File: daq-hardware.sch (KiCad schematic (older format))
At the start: 29 parts, among them J1 USB_B, J2 Micro_SD_Card_Det_Hirose_DM3AT, Q1 MMDT2222A, SW1 SW1, SW2 SW1, U1 CP2102N-A01-GQFN24, U2 ESP32-WROOM-32D

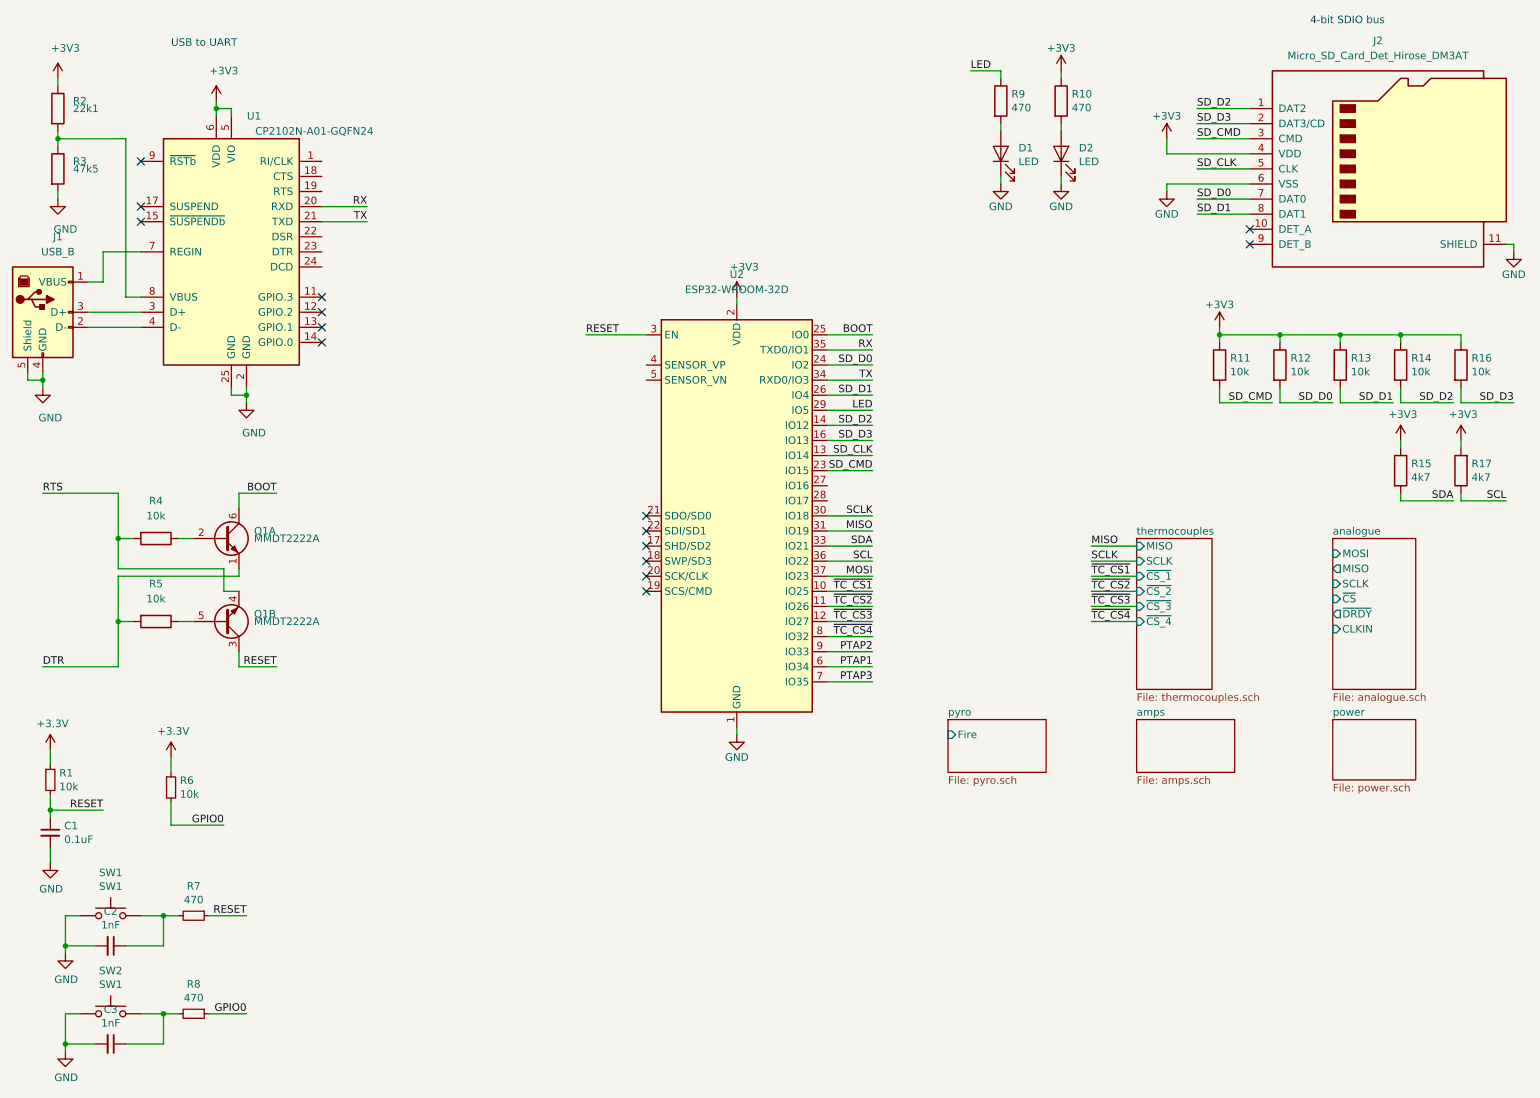
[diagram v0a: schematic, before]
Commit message: Fixed conflicts, assigned all footprints.
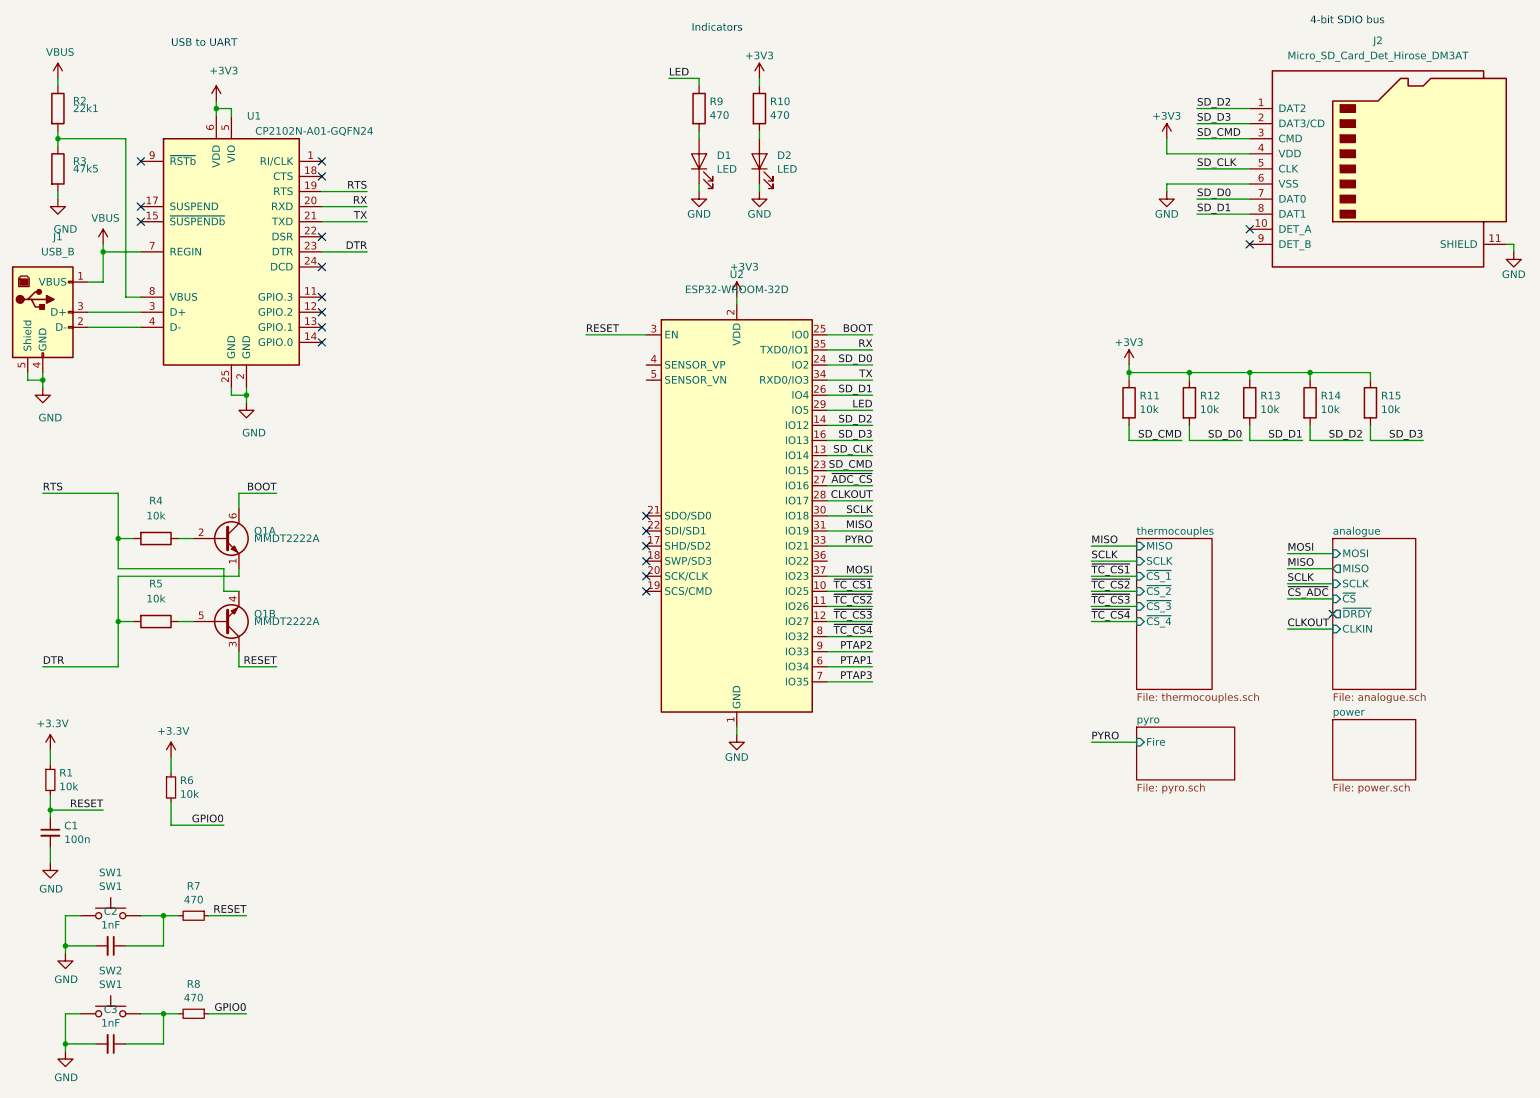
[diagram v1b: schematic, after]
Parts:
- removed R15, R17: 4k7, symbol Device:R
- C1: value 0.1uF -> 100n; footprint (none) -> Capacitor_SMD:C_0603_1608Metric
- C2, C3: footprint (none) -> Capacitor_SMD:C_0603_1608Metric
- D1, D2: footprint (none) -> Diode_SMD:D_0603_1608Metric_Castellated
- R1, R10, R11, R12, R13, R14, R2, R3, R6, R7, R8, R9: footprint (none) -> Resistor_SMD:R_0603_1608Metric
- R15: renamed from R16; footprint (none) -> Resistor_SMD:R_0603_1608Metric
- SW1, SW2: footprint (none) -> Button_Switch_SMD:SW_Push_1P1T_NO_CK_KMR2
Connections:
- net +3V3: no longer R2.1
- net DTR: now also U1.23 (DTR)
- net RTS: now also U1.19 (RTS)
- net ~ADC_CS: now reaches U2.27 (IO16)
- net CLKOUT: now reaches U2.28 (IO17)
- net VBUS: now reaches J1.1 (VBUS), U1.7 (REGIN)
- net VBUS: now also R2.1
- net SCL: no longer names the net of U2.36 (IO22)
- net SDA renamed PYRO
- no-connect marks 15 -> 20
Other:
- note added: "Indicators"
- moved on the sheet: D1, D2, R10, R11, R12, R13, R14, R15, R9

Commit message: Cleaned up layout, added barrel jack for power input
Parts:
- U1: footprint Package_DFN_QFN:QFN-24-1EP_4x4mm_P0.5mm_EP2.6x2.6mm -> Package_DFN_QFN:QFN-24-1EP_4x4mm_P0.5mm_EP2.6x2.6mm_ThermalVias
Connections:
- net ~TC_CS1: now also U2.12 (IO27); no longer U2.10 (IO25)
- net ~TC_CS3: now also U2.10 (IO25); no longer U2.12 (IO27)
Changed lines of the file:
@@
 F 0 "U1" H 2750 3050 50  0000 C CNN
 F 1 "CP2102N-A01-GQFN24" H 3150 2950 50  0000 C CNN
-F 2 "Package_DFN_QFN:QFN-24-1EP_4x4mm_P0.5mm_EP2.6x2.6mm" H 3050 1350 50  0001 L CNN
+F 2 "Package_DFN_QFN:QFN-24-1EP_4x4mm_P0.5mm_EP2.6x2.6mm_ThermalVias" H 3050 1350 50  0001 L CNN
 F 3 "https://www.silabs.com/documents/public/data-sheets/cp2102n-datasheet.pdf" H 2650 1100 50  0001 C CNN
 	1    2600 2150
@@
 4-bit SDIO bus
 Wire Wire Line
-	6550 4400 6850 4400
-Wire Wire Line
 	6550 4500 6850 4500
-Text Label 6850 4400 2    50   ~ 0
-~TC_CS1
 Text Label 6850 4500 2    50   ~ 0
 ~TC_CS2
@@
 PTAP3
 Wire Wire Line
-	6550 4600 6850 4600
-Text Label 6850 4600 2    50   ~ 0
+	6550 4400 6850 4400
+Text Label 6850 4400 2    50   ~ 0
 ~TC_CS3
 Wire Wire Line
@@
 NoConn ~ 3200 1650
 NoConn ~ 3200 1550
+Wire Wire Line
+	6550 4600 6850 4600
+Text Label 6850 4600 2    50   ~ 0
+~TC_CS1
 $EndSCHEMATC

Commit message: Laid out +3V3 section
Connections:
- net BOOT: now also R8.1
- net GPIO0: no longer R8.1
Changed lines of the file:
@@
 RESET
 Text Label 2700 7200 2    50   ~ 0
-GPIO0
+BOOT
 $Sheet
 S 9900 5250 550  400

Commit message: Added 3D models, added ptaps sheet, fixed pyros
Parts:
- R2: value 22k1 -> 22k
- R3: value 47k5 -> 43k
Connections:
- net CONT: now reaches U2.36 (IO22)
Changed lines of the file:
@@
 $Descr A4 11693 8268
 encoding utf-8
-Sheet 1 5
+Sheet 1 6
 Title ""
 Date ""
@@
 P 1450 1200
 F 0 "R2" H 1550 1250 50  0000 L CNN
-F 1 "22k1" H 1550 1200 50  0000 L CNN
+F 1 "22k" H 1550 1200 50  0000 L CNN
 F 2 "Resistor_SMD:R_0603_1608Metric" V 1380 1200 50  0001 C CNN
 F 3 "~" H 1450 1200 50  0001 C CNN
@@
 P 1450 1600
 F 0 "R3" H 1550 1650 50  0000 L CNN
-F 1 "47k5" H 1550 1600 50  0000 L CNN
+F 1 "43k" H 1550 1600 50  0000 L CNN
 F 2 "Resistor_SMD:R_0603_1608Metric" V 1380 1600 50  0001 C CNN
 F 3 "~" H 1450 1600 50  0001 C CNN
@@
 F1 "pyro.sch" 50
 F2 "Fire" I L 8600 5400 50
+F3 "Cont" O L 8600 5500 50
 $EndSheet
 $Sheet
@@
 Text Label 6850 4600 2    50   ~ 0
 ~TC_CS1
+Wire Wire Line
+	6550 4200 6850 4200
+Text Label 6850 4200 2    50   ~ 0
+CONT
+Wire Wire Line
+	8600 5500 8300 5500
+Text Label 8300 5500 0    50   ~ 0
+CONT
+$Sheet
+S 7600 5300 500  350
+U 5DD033F3
+F0 "ptaps" 50
+F1 "ptaps.sch" 50
+F2 "PTAP1" O L 7600 5350 50
+F3 "PTAP2" O L 7600 5450 50
+F4 "PTAP3" O L 7600 5550 50
+$EndSheet
 $EndSCHEMATC

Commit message: Release candidate
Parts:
- removed C1: 100n, Capacitor_SMD:C_0603_1608Metric, symbol Device:C_Small
- removed R1, R6: 10k, Resistor_SMD:R_0603_1608Metric, symbol Device:R_Small
- added J35: Conn_01x04, Connector_PinHeader_2.54mm:PinHeader_1x04_P2.54mm_Vertical, symbol Connector_Generic:Conn_01x04
- added R1, R6: 4k7, Resistor_SMD:R_0603_1608Metric, symbol Device:R
- D1: footprint Diode_SMD:D_0603_1608Metric_Castellated -> LED_SMD:LED_0603_1608Metric_Castellated
- U2: footprint RF_Module:ESP32-WROOM-32 -> RF_Module:ESP32-WROOM-32U
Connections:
- net +3V3: now also J35.3 (Pin_3), R1.1, R6.1
- net CONT: now also U2.26 (IO4); no longer U2.36 (IO22)
- net GND: now also J35.4 (Pin_4)
- net PTAP1: now also U2.9 (IO33); no longer U2.6 (IO34)
- net PTAP2: now also U2.7 (IO35); no longer U2.9 (IO33)
- net PTAP3: now also U2.6 (IO34); no longer U2.7 (IO35)
- net PYRO: now also U2.14 (IO12); no longer U2.33 (IO21)
- net SD_D1: no longer U2.26 (IO4)
- net SD_D2: no longer U2.14 (IO12)
- net SD_CMD renamed SD_MOSI
- net SD_D0 renamed SD_MISO
- net SD_D3 renamed SD_CS
- new net SCL: J35.2 (Pin_2), R6.2, U2.36 (IO22)
- new net SDA: J35.1 (Pin_1), R1.2, U2.33 (IO21)
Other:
- moved on the sheet: R11, R12, R13, R14, R15

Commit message: Edward appeasement
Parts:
- added J38: Conn_01x02, Connector_PinHeader_2.54mm:PinHeader_1x02_P2.54mm_Vertical, symbol Connector_Generic:Conn_01x02
- D2: footprint Diode_SMD:D_0603_1608Metric_Castellated -> LED_SMD:LED_0603_1608Metric_Castellated
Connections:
- net SENSVP: now reaches U2.4 (SENSOR_VP)
- net SENSVP: now also J38.1 (Pin_1)
- net SENSVN: now reaches U2.5 (SENSOR_VN)
- net SENSVN: now also J38.2 (Pin_2)
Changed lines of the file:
@@
 RX
 Wire Wire Line
-	6550 2800 6850 2800
-Wire Wire Line
-	6550 3000 6850 3000
-Text Label 6850 2800 2    50   ~ 0
+	6550 2800 6900 2800
+Wire Wire Line
+	6550 3000 6900 3000
+Text Label 6900 2800 2    50   ~ 0
 RX
-Text Label 6850 3000 2    50   ~ 0
+Text Label 6900 3000 2    50   ~ 0
 TX
 $Comp
@@
 RESET
 Wire Wire Line
-	6550 2700 6850 2700
-Text Label 6850 2700 2    50   ~ 0
+	6550 2700 6900 2700
+Text Label 6900 2700 2    50   ~ 0
 BOOT
 NoConn ~ 9350 2100
@@
 SD_MISO
 Wire Wire Line
-	6850 3900 6550 3900
-Wire Wire Line
-	6850 4000 6550 4000
-Wire Wire Line
-	6850 4300 6550 4300
-Text Label 6850 3900 2    50   ~ 0
+	6900 3900 6550 3900
+Wire Wire Line
+	6900 4000 6550 4000
+Wire Wire Line
+	6900 4300 6550 4300
+Text Label 6900 3900 2    50   ~ 0
 SCLK
-Text Label 6850 4000 2    50   ~ 0
+Text Label 6900 4000 2    50   ~ 0
 MISO
-Text Label 6850 4300 2    50   ~ 0
+Text Label 6900 4300 2    50   ~ 0
 MOSI
 $Comp
@@
 $EndSheet
 Wire Wire Line
-	6550 2900 6850 2900
-Text Label 6850 2900 2    50   ~ 0
+	6550 2900 6900 2900
+Text Label 6900 2900 2    50   ~ 0
 SD_MISO
 Wire Wire Line
-	6550 3400 6850 3400
-Wire Wire Line
-	6550 3500 6850 3500
-Wire Wire Line
-	6550 3600 6850 3600
-Text Label 6850 3400 2    50   ~ 0
+	6550 3400 6900 3400
+Wire Wire Line
+	6550 3500 6900 3500
+Wire Wire Line
+	6550 3600 6900 3600
+Text Label 6900 3400 2    50   ~ 0
 SD_CS
-Text Label 6850 3600 2    50   ~ 0
+Text Label 6900 3600 2    50   ~ 0
 SD_MOSI
-Text Label 6850 3500 2    50   ~ 0
+Text Label 6900 3500 2    50   ~ 0
 SD_CLK
 $Comp
@@
 4-bit SDIO bus
 Wire Wire Line
-	6550 4500 6850 4500
-Text Label 6850 4500 2    50   ~ 0
+	6550 4500 6900 4500
+Text Label 6900 4500 2    50   ~ 0
 ~TC_CS2
 Text Label 8300 4100 0    50   ~ 0
@@
 	8300 4400 8600 4400
 Wire Wire Line
-	6550 4800 6850 4800
-Wire Wire Line
-	6550 5000 6850 5000
-Text Label 6850 4800 2    50   ~ 0
+	6550 4800 6900 4800
+Wire Wire Line
+	6550 5000 6900 5000
+Text Label 6900 4800 2    50   ~ 0
 PTAP1
-Text Label 6850 5000 2    50   ~ 0
+Text Label 6900 5000 2    50   ~ 0
 PTAP2
 Wire Wire Line
-	6550 4900 6850 4900
-Text Label 6850 4900 2    50   ~ 0
+	6550 4900 6900 4900
+Text Label 6900 4900 2    50   ~ 0
 PTAP3
 Wire Wire Line
-	6550 4400 6850 4400
-Text Label 6850 4400 2    50   ~ 0
+	6550 4400 6900 4400
+Text Label 6900 4400 2    50   ~ 0
 ~TC_CS3
 Wire Wire Line
-	6550 4700 6850 4700
-Text Label 6850 4700 2    50   ~ 0
+	6550 4700 6900 4700
+Text Label 6900 4700 2    50   ~ 0
 ~TC_CS4
 Wire Wire Line
@@
 F 0 "D2" V 6139 1433 50  0000 R CNN
 F 1 "LED" V 6048 1433 50  0000 R CNN
-F 2 "Diode_SMD:D_0603_1608Metric_Castellated" H 6100 1550 50  0001 C CNN
+F 2 "LED_SMD:LED_0603_1608Metric_Castellated" H 6100 1550 50  0001 C CNN
 F 3 "~" H 6100 1550 50  0001 C CNN
 	1    6100 1550
@@
 LED
 Wire Wire Line
-	6550 3200 6850 3200
-Text Label 6850 3200 2    50   ~ 0
+	6550 3200 6900 3200
+Text Label 6900 3200 2    50   ~ 0
 LED
 $Sheet
@@
 $EndSheet
 Wire Wire Line
-	6550 3800 6850 3800
-Text Label 6850 3800 2    50   ~ 0
+	6550 3800 6900 3800
+Text Label 6900 3800 2    50   ~ 0
 CLKOUT
 Wire Wire Line
@@
 CLKOUT
 Wire Wire Line
-	6550 3700 6850 3700
-Text Label 6850 3700 2    50   ~ 0
+	6550 3700 6900 3700
+Text Label 6900 3700 2    50   ~ 0
 ~ADC_CS
 Text Label 9600 4450 0    50   ~ 0
@@
 NoConn ~ 3200 1550
 Wire Wire Line
-	6550 4600 6850 4600
-Text Label 6850 4600 2    50   ~ 0
+	6550 4600 6900 4600
+Text Label 6900 4600 2    50   ~ 0
 ~TC_CS1
 Wire Wire Line
@@
 CONT
 $Sheet
-S 7600 5300 500  350
+S 7600 5300 550  700
 U 5DD033F3
 F0 "ptaps" 50
@@
 F3 "PTAP2" O L 7600 5450 50
 F4 "PTAP3" O L 7600 5550 50
+F5 "PTAP4" O L 7600 5650 50
+F6 "PTAP5" O L 7600 5750 50
 $EndSheet
 $Sheet
@@
 $EndSheet
 Wire Wire Line
-	6550 4100 6850 4100
-Wire Wire Line
-	6550 4200 6850 4200
-Text Label 6850 4100 2    50   ~ 0
+	6550 4100 6900 4100
+Wire Wire Line
+	6550 4200 6900 4200
+Text Label 6900 4100 2    50   ~ 0
 SDA
-Text Label 6850 4200 2    50   ~ 0
+Text Label 6900 4200 2    50   ~ 0
 SCL
 Wire Wire Line
-	6550 3100 6850 3100
-Wire Wire Line
-	6550 3300 6850 3300
-Text Label 6850 3300 2    50   ~ 0
+	6550 3100 6900 3100
+Wire Wire Line
+	6550 3300 6900 3300
+Text Label 6900 3300 2    50   ~ 0
 PYRO
-Text Label 6850 3100 2    50   ~ 0
+Text Label 6900 3100 2    50   ~ 0
 CONT
 Wire Wire Line
@@
 Text Label 9750 3350 0    50   ~ 0
 SCL
+$Comp
+L Connector_Generic:Conn_01x02 J38
+U 1 1 5E14F78B
+P 4750 2900
+F 0 "J38" H 4668 3117 50  0000 C CNN
+F 1 "Conn_01x02" H 4668 3026 50  0000 C CNN
+F 2 "Connector_PinHeader_2.54mm:PinHeader_1x02_P2.54mm_Vertical" H 4750 2900 50  0001 C CNN
+F 3 "~" H 4750 2900 50  0001 C CNN
+	1    4750 2900
+	-1   0    0    -1
+$EndComp
+Wire Wire Line
+	4950 2900 5350 2900
+Wire Wire Line
+	4950 3000 5350 3000
+Text Label 4950 2900 0    50   ~ 0
+SENSVP
+Text Label 4950 3000 0    50   ~ 0
+SENSVN
+Wire Wire Line
+	7600 5650 7300 5650
+Wire Wire Line
+	7300 5750 7600 5750
+Text Label 7300 5650 0    50   ~ 0
+SENSVN
+Text Label 7300 5750 0    50   ~ 0
+SENSVP
 $EndSCHEMATC
